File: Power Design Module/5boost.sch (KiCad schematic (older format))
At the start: 15 parts, among them J1 105430-1102, J2 105430-1102, J3 105430-1102, U1 TPS61232DRCR, U2 TPPM0110DWPR

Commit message: Finalized Charge board
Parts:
- C1, C5, C6: Allied Price/Stock https://www.digikey.com/product-detail/en/murata-electronic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 -> (none); Manfacturing # (none) -> GRM188R61A106KE69J; Manufacturer_Name Murata -> (none); Manufacturer_Part_Number GRM188R61A106KE69J -> (none); Mouser Price/Stock https://www.digikey.com/product-detail/en/murata-electronic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 -> (none)
- C2, C3, C4: Allied Price/Stock https://www.digikey.com/product-detail/en/kemet/C0201C101J3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 -> (none); Manfacturing # (none) -> C0201C101J3GACTU; Manufacturer_Name KEMET -> (none); Manufacturer_Part_Number C0201C101J3GACTU -> (none); Mouser Price/Stock https://www.digikey.com/product-detail/en/kemet/C0201C101J3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 -> (none)
- J1, J2, J3: Allied Price/Stock https://www.alliedelec.com/molexincorporated-105430-1102/71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 -> (none); Allied_Number 71607964 -> (none); Height 6.99 -> (none); Manfacturing # (none) -> 105430-1102; Manufacturer_Name Molex -> (none); Manufacturer_Part_Number 105430-1102 -> (none); Mouser Part Number 538-105430-1102 -> (none); Mouser Price/Stock https://www.mouser.com/Search/Refine.aspx?Keyword=538-10543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 -> (none)

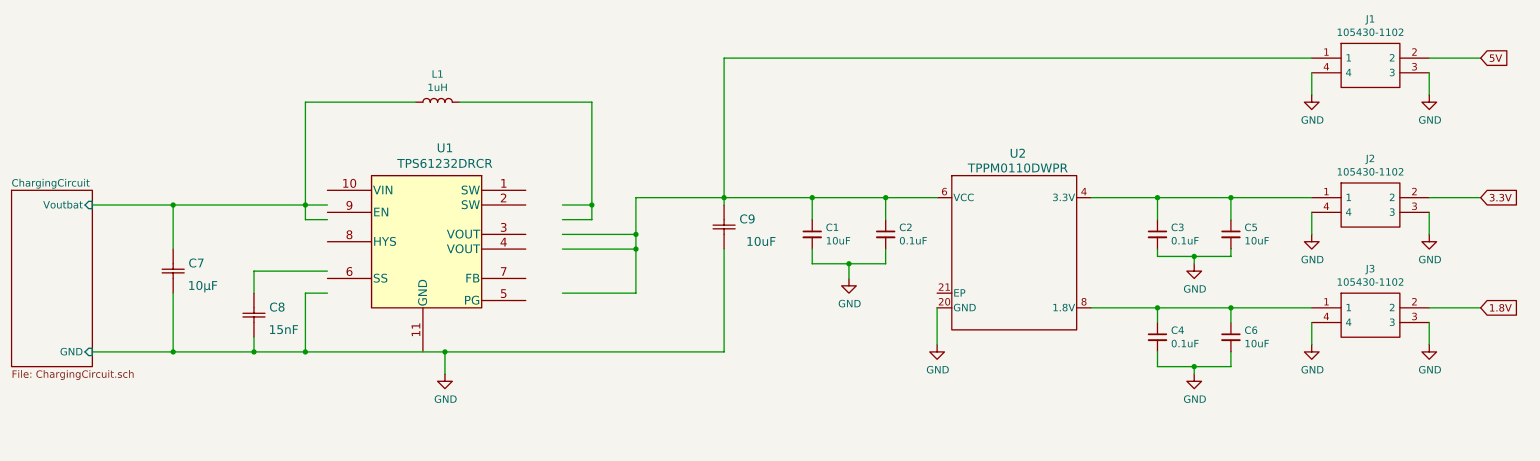
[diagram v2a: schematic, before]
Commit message: Starting Power board Layout. Design Changes
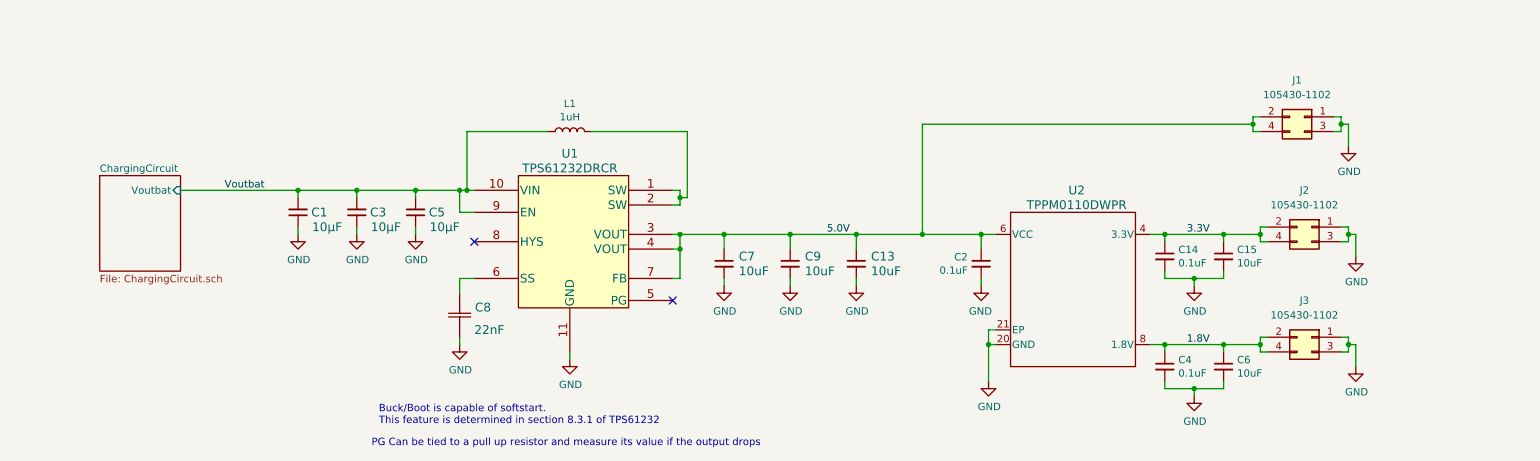
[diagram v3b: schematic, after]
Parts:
- removed C7: 10μF, Capacitor_SMD:C_0603_1608Metric_Pad1.05x0.95mm_HandSolder, symbol 5boost-rescue:C1608X5R1A106M080AC-C1608X5R1A106M080AC
- removed C9: 10uF, Capacitor_SMD:C_0805_2012Metric_Pad1.15x1.40mm_HandSolder, symbol 5boost-rescue:C2012X7R1A106M125AC-C2012X7R1A106M125AC
- removed J1, J2, J3: 105430-1102, 105430-1102:1054301102, symbol MOLEX_Connector_105430:105430-1102
- added C13, C7, C9: 10uF, Capacitor_SMD:C_0805_2012Metric_Pad1.15x1.40mm_HandSolder, symbol Device:C_Small
- added C14: 0.1uF, Capacitor_SMD:C_0603_1608Metric_Pad1.05x0.95mm_HandSolder, symbol Device:C_Small
- added C15: 10uF, Capacitor_SMD:C_0603_1608Metric_Pad1.05x0.95mm_HandSolder, symbol Device:C_Small
- added J1, J2, J3: 105430-1102, 105430-1102:1054301102, symbol Connector_Generic:Conn_02x02_Odd_Even
- C1, C5: value 10uF -> 10μF; Description 10µF ±10% 10V Ceramic Capacitor X5R 0603 (1608 Metric) -> (none); Manfacturing # GRM188R61A106KE69J -> CL10B106MQ8NRNC
- C3: value 0.1uF -> 10μF; Description 100pF ±5% 25V Ceramic Capacitor C0G, NP0 0201 (0603 Metric) -> (none); Manfacturing # C0201C101J3GACTU -> CL10B106MQ8NRNC
- C8: value 15nF -> 22nF; Manfacturing # (none) -> C0603C223K4RACTU
- L1: Manfacturing # (none) -> IHLP2020BZER1R0M01
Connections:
- net labels added: 5.0V, Voutbat
- net labels removed: 5V
- wire segments 76 -> 102
- no-connect marks 0 -> 2
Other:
- note added: "Buck/Boot is capable of softstart.\nThis feature is determined in section 8.3.1 of TPS61232"
- note added: "PG Can be tied to a pull up resistor and measure its value if the output drops"
- moved on the sheet: C2, C4, C6, C8, L1, U1, U2

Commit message: Final Power Breakout completed. Headers were used instead of the previous Molex Connectors
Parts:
- removed J2, J3: 105430-1102, 105430-1102:1054301102, symbol Connector_Generic:Conn_02x02_Odd_Even
- added J2: 3.3V, Connector_PinSocket_2.54mm:PinSocket_2x02_P2.54mm_Vertical, symbol Connector_Generic:Conn_02x02_Counter_Clockwise
- added J3: 1.8V, Connector_PinSocket_2.54mm:PinSocket_2x02_P2.54mm_Vertical, symbol Connector_Generic:Conn_02x02_Counter_Clockwise
- C15, C6: Manfacturing # GRM188R61A106KE69J -> GRM188R61A106KE69D
- J1: value 105430-1102 -> 5.0V; footprint 105430-1102:1054301102 -> Connector_PinSocket_2.54mm:PinSocket_2x02_P2.54mm_Vertical; symbol Connector_Generic:Conn_02x02_Odd_Even -> Connector_Generic:Conn_02x02_Counter_Clockwise
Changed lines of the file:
@@
 F 7 "" H 9050 4450 50  0001 C CNN "Manufacturer_Part_Number"
 F 8 "" H 9050 4450 50  0001 C CNN "Mouser Price/Stock"
-F 9 "GRM188R61A106KE69J" H 9050 4450 50  0001 C CNN "Manfacturing #"
+F 9 "GRM188R61A106KE69D" H 9050 4450 50  0001 C CNN "Manfacturing #"
 	1    9050 4450
 	1    0    0    -1
@@
 $EndComp
 Connection ~ 5350 3550
-$Comp
-L Connector_Generic:Conn_02x02_Odd_Even J3
-U 1 1 5E40F2B1
-P 9650 4250
-F 0 "J3" H 9700 4500 50  0000 C CNN
-F 1 "105430-1102" H 9700 4400 50  0000 C CNN
-F 2 "105430-1102:1054301102" H 10300 4350 50  0001 L CNN
-F 3 "https://www.molex.com/pdm_docs/sd/1054301102_sd.pdf" H 10300 4250 50  0001 L CNN
-F 4 "" H 9650 4250 50  0001 C CNN "Allied Price/Stock"
-F 5 "" H 9650 4250 50  0001 C CNN "Allied_Number"
-F 6 "MOLEX - 105430-1102 - NANO-FIT HDR SMT RA SGL 2CKT TIN BLK 84AC4685" H 9650 4250 50  0001 C CNN "Description"
-F 7 "" H 9650 4250 50  0001 C CNN "Height"
-F 8 "" H 9650 4250 50  0001 C CNN "Manufacturer_Name"
-F 9 "" H 9650 4250 50  0001 C CNN "Manufacturer_Part_Number"
-F 10 "" H 9650 4250 50  0001 C CNN "Mouser Part Number"
-F 11 "" H 9650 4250 50  0001 C CNN "Mouser Price/Stock"
-F 12 "105430-1102" H 9650 4250 50  0001 C CNN "Manfacturing #"
-	1    9650 4250
-	-1   0    0    -1
-$EndComp
 Wire Wire Line
 	8550 4300 8650 4300
@@
 F 7 "" H 9050 3700 50  0001 C CNN "Manufacturer_Part_Number"
 F 8 "" H 9050 3700 50  0001 C CNN "Mouser Price/Stock"
-F 9 "GRM188R61A106KE69J" H 9050 3700 50  0001 C CNN "Manfacturing #"
+F 9 "GRM188R61A106KE69D" H 9050 3700 50  0001 C CNN "Manfacturing #"
 	1    9050 3700
 	1    0    0    -1
@@
 	1    8850 3900
 	1    0    0    -1
-$EndComp
-$Comp
-L Connector_Generic:Conn_02x02_Odd_Even J2
-U 1 1 5E43CF7F
-P 9650 3500
-F 0 "J2" H 9700 3750 50  0000 C CNN
-F 1 "105430-1102" H 9700 3650 50  0000 C CNN
-F 2 "105430-1102:1054301102" H 10300 3600 50  0001 L CNN
-F 3 "https://www.molex.com/pdm_docs/sd/1054301102_sd.pdf" H 10300 3500 50  0001 L CNN
-F 4 "" H 9650 3500 50  0001 C CNN "Allied Price/Stock"
-F 5 "" H 9650 3500 50  0001 C CNN "Allied_Number"
-F 6 "MOLEX - 105430-1102 - NANO-FIT HDR SMT RA SGL 2CKT TIN BLK 84AC4685" H 9650 3500 50  0001 C CNN "Description"
-F 7 "" H 9650 3500 50  0001 C CNN "Height"
-F 8 "" H 9650 3500 50  0001 C CNN "Manufacturer_Name"
-F 9 "" H 9650 3500 50  0001 C CNN "Manufacturer_Part_Number"
-F 10 "" H 9650 3500 50  0001 C CNN "Mouser Part Number"
-F 11 "" H 9650 3500 50  0001 C CNN "Mouser Price/Stock"
-F 12 "105430-1102" H 9650 3500 50  0001 C CNN "Manfacturing #"
-	1    9650 3500
-	-1   0    0    -1
 $EndComp
 Wire Wire Line
@@
 	3550 3300 3550 3250
 $Comp
-L Connector_Generic:Conn_02x02_Odd_Even J1
+L Connector_Generic:Conn_02x02_Counter_Clockwise J1
 U 1 1 5E4C441F
-P 9600 2750
-F 0 "J1" H 9650 3000 50  0000 C CNN
-F 1 "105430-1102" H 9650 2900 50  0000 C CNN
-F 2 "105430-1102:1054301102" H 10250 2850 50  0001 L CNN
-F 3 "https://www.molex.com/pdm_docs/sd/1054301102_sd.pdf" H 10250 2750 50  0001 L CNN
-F 4 "" H 9600 2750 50  0001 C CNN "Allied Price/Stock"
-F 5 "" H 9600 2750 50  0001 C CNN "Allied_Number"
-F 6 "MOLEX - 105430-1102 - NANO-FIT HDR SMT RA SGL 2CKT TIN BLK 84AC4685" H 9600 2750 50  0001 C CNN "Description"
-F 7 "" H 9600 2750 50  0001 C CNN "Height"
-F 8 "" H 9600 2750 50  0001 C CNN "Manufacturer_Name"
-F 9 "" H 9600 2750 50  0001 C CNN "Manufacturer_Part_Number"
-F 10 "" H 9600 2750 50  0001 C CNN "Mouser Part Number"
-F 11 "" H 9600 2750 50  0001 C CNN "Mouser Price/Stock"
-F 12 "105430-1102" H 9600 2750 50  0001 C CNN "Manfacturing #"
-	1    9600 2750
-	-1   0    0    -1
-$EndComp
-Wire Wire Line
-	9300 2750 9250 2750
-Wire Wire Line
-	9250 2750 9250 2800
-Wire Wire Line
-	9250 2850 9300 2850
-Connection ~ 9250 2800
-Wire Wire Line
-	9250 2800 9250 2850
-Wire Wire Line
-	9800 2750 9850 2750
-Wire Wire Line
-	9850 2750 9850 2800
-Wire Wire Line
-	9850 2850 9800 2850
+P 9550 2750
+F 0 "J1" H 9600 3000 50  0000 C CNN
+F 1 "5.0V" H 9600 2900 50  0000 C CNN
+F 2 "Connector_PinSocket_2.54mm:PinSocket_2x02_P2.54mm_Vertical" H 10200 2850 50  0001 L CNN
+F 3 "" H 10200 2750 50  0001 L CNN
+F 4 "" H 9550 2750 50  0001 C CNN "Allied Price/Stock"
+F 5 "" H 9550 2750 50  0001 C CNN "Allied_Number"
+F 6 "MOLEX - 105430-1102 - NANO-FIT HDR SMT RA SGL 2CKT TIN BLK 84AC4685" H 9550 2750 50  0001 C CNN "Description"
+F 7 "" H 9550 2750 50  0001 C CNN "Height"
+F 8 "" H 9550 2750 50  0001 C CNN "Manufacturer_Name"
+F 9 "" H 9550 2750 50  0001 C CNN "Manufacturer_Part_Number"
+F 10 "" H 9550 2750 50  0001 C CNN "Mouser Part Number"
+F 11 "" H 9550 2750 50  0001 C CNN "Mouser Price/Stock"
+F 12 "105430-1102" H 9550 2750 50  0001 C CNN "Manfacturing #"
+	1    9550 2750
+	1    0    0    -1
+$EndComp
+Wire Wire Line
+	9350 2750 9300 2750
+Wire Wire Line
+	9850 2750 9900 2750
+Wire Wire Line
+	9900 2750 9900 2800
+Wire Wire Line
+	9900 2850 9850 2850
 $Comp
 L power:GND #PWR0127
 U 1 1 5E4C442E
-P 9900 2950
-F 0 "#PWR0127" H 9900 2700 50  0001 C CNN
-F 1 "GND" H 9905 2777 50  0000 C CNN
-F 2 "" H 9900 2950 50  0001 C CNN
-F 3 "" H 9900 2950 50  0001 C CNN
-	1    9900 2950
-	1    0    0    -1
-$EndComp
-Wire Wire Line
-	9850 2800 9900 2800
-Connection ~ 9850 2800
-Wire Wire Line
-	9850 2800 9850 2850
-Wire Wire Line
-	9900 2800 9900 2950
+P 9950 2950
+F 0 "#PWR0127" H 9950 2700 50  0001 C CNN
+F 1 "GND" H 9955 2777 50  0000 C CNN
+F 2 "" H 9950 2950 50  0001 C CNN
+F 3 "" H 9950 2950 50  0001 C CNN
+	1    9950 2950
+	1    0    0    -1
+$EndComp
+Wire Wire Line
+	9900 2800 9950 2800
+Connection ~ 9900 2800
+Wire Wire Line
+	9900 2800 9900 2850
 Wire Wire Line
 	7000 2800 7000 3550
-Wire Wire Line
-	7000 2800 9250 2800
 Connection ~ 7000 3550
 Wire Wire Line
@@
 Wire Wire Line
 	3550 3250 3850 3250
+Wire Wire Line
+	9300 2750 9300 2800
+Wire Wire Line
+	9300 2850 9350 2850
+Wire Wire Line
+	9300 2800 7000 2800
+Connection ~ 9300 2800
+Wire Wire Line
+	9300 2800 9300 2850
+Wire Wire Line
+	9950 2800 9950 2950
+$Comp
+L Connector_Generic:Conn_02x02_Counter_Clockwise J3
+U 1 1 5E3214E3
+P 9550 4250
+F 0 "J3" H 9600 4500 50  0000 C CNN
+F 1 "1.8V" H 9600 4400 50  0000 C CNN
+F 2 "Connector_PinSocket_2.54mm:PinSocket_2x02_P2.54mm_Vertical" H 10200 4350 50  0001 L CNN
+F 3 "" H 10200 4250 50  0001 L CNN
+F 4 "" H 9550 4250 50  0001 C CNN "Allied Price/Stock"
+F 5 "" H 9550 4250 50  0001 C CNN "Allied_Number"
+F 6 "MOLEX - 105430-1102 - NANO-FIT HDR SMT RA SGL 2CKT TIN BLK 84AC4685" H 9550 4250 50  0001 C CNN "Description"
+F 7 "" H 9550 4250 50  0001 C CNN "Height"
+F 8 "" H 9550 4250 50  0001 C CNN "Manufacturer_Name"
+F 9 "" H 9550 4250 50  0001 C CNN "Manufacturer_Part_Number"
+F 10 "" H 9550 4250 50  0001 C CNN "Mouser Part Number"
+F 11 "" H 9550 4250 50  0001 C CNN "Mouser Price/Stock"
+F 12 "105430-1102" H 9550 4250 50  0001 C CNN "Manfacturing #"
+	1    9550 4250
+	1    0    0    -1
+$EndComp
+$Comp
+L Connector_Generic:Conn_02x02_Counter_Clockwise J2
+U 1 1 5E321C74
+P 9550 3500
+F 0 "J2" H 9600 3750 50  0000 C CNN
+F 1 "3.3V" H 9600 3650 50  0000 C CNN
+F 2 "Connector_PinSocket_2.54mm:PinSocket_2x02_P2.54mm_Vertical" H 10200 3600 50  0001 L CNN
+F 3 "" H 10200 3500 50  0001 L CNN
+F 4 "" H 9550 3500 50  0001 C CNN "Allied Price/Stock"
+F 5 "" H 9550 3500 50  0001 C CNN "Allied_Number"
+F 6 "MOLEX - 105430-1102 - NANO-FIT HDR SMT RA SGL 2CKT TIN BLK 84AC4685" H 9550 3500 50  0001 C CNN "Description"
+F 7 "" H 9550 3500 50  0001 C CNN "Height"
+F 8 "" H 9550 3500 50  0001 C CNN "Manufacturer_Name"
+F 9 "" H 9550 3500 50  0001 C CNN "Manufacturer_Part_Number"
+F 10 "" H 9550 3500 50  0001 C CNN "Mouser Part Number"
+F 11 "" H 9550 3500 50  0001 C CNN "Mouser Price/Stock"
+F 12 "105430-1102" H 9550 3500 50  0001 C CNN "Manfacturing #"
+	1    9550 3500
+	1    0    0    -1
+$EndComp
 $EndSCHEMATC
